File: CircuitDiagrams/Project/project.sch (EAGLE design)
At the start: 19 parts, among them IC1 UC3C, IC2 PCA9542A, IC3 MT48LC4M16A2TSOP54, Q1 OV7670, Q2 OV7670, X1 SDBMF

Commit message: Done some more to the PCB. Worked out how to use the cam2print script
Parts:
- added C1, C2: 22pF, passives:C-EUC1206
- added C3, C4: 10uF, passives:CPOL-EUSMCE
- added IC4, IC5: TB6593FNGSSOP20, ICs:TB6593FNGSSOP20
- added J2, J3: 1BY2THROUGHHOLE, Headers:1BY2THROUGHHOLE
- added Q3: VREGSOT-223, Semiconductors:VREGSOT-223
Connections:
- removed net VBUS: IC1.VBUS, U$1.VBUS
- new net +5V: C4.+, IC1.VBUS, Q3.VIN, U$1.VBUS
- new net N$1: IC5.O1, IC5.O11, J3.1
- new net N$2: IC5.O2, IC5.O22, J3.2
- new net N$3: IC4.O2, IC4.O22, J2.2
- new net N$4: IC4.O1, IC4.O11, J2.1
- net +3V3: now also C3.+, IC4.VCC, IC4.VM1, IC4.VM2, IC4.VM3, IC4.VM4, IC5.VCC, IC5.VM1, IC5.VM2, IC5.VM3, IC5.VM4, Q3.VOUT
- net GND: now also C3.-, C4.-, IC4.GND, IC4.PGND1, IC4.PGND2, IC4.PGND3, IC4.PGND4, IC4.PGND5, IC4.PGND6, IC5.GND, IC5.PGND1, IC5.PGND2, IC5.PGND3, IC5.PGND4, IC5.PGND5, IC5.PGND6, Q3.GND
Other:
- note added: "Motor Drivers"
- note added: "SDRAM"
- note added: "Voltage Regulator"

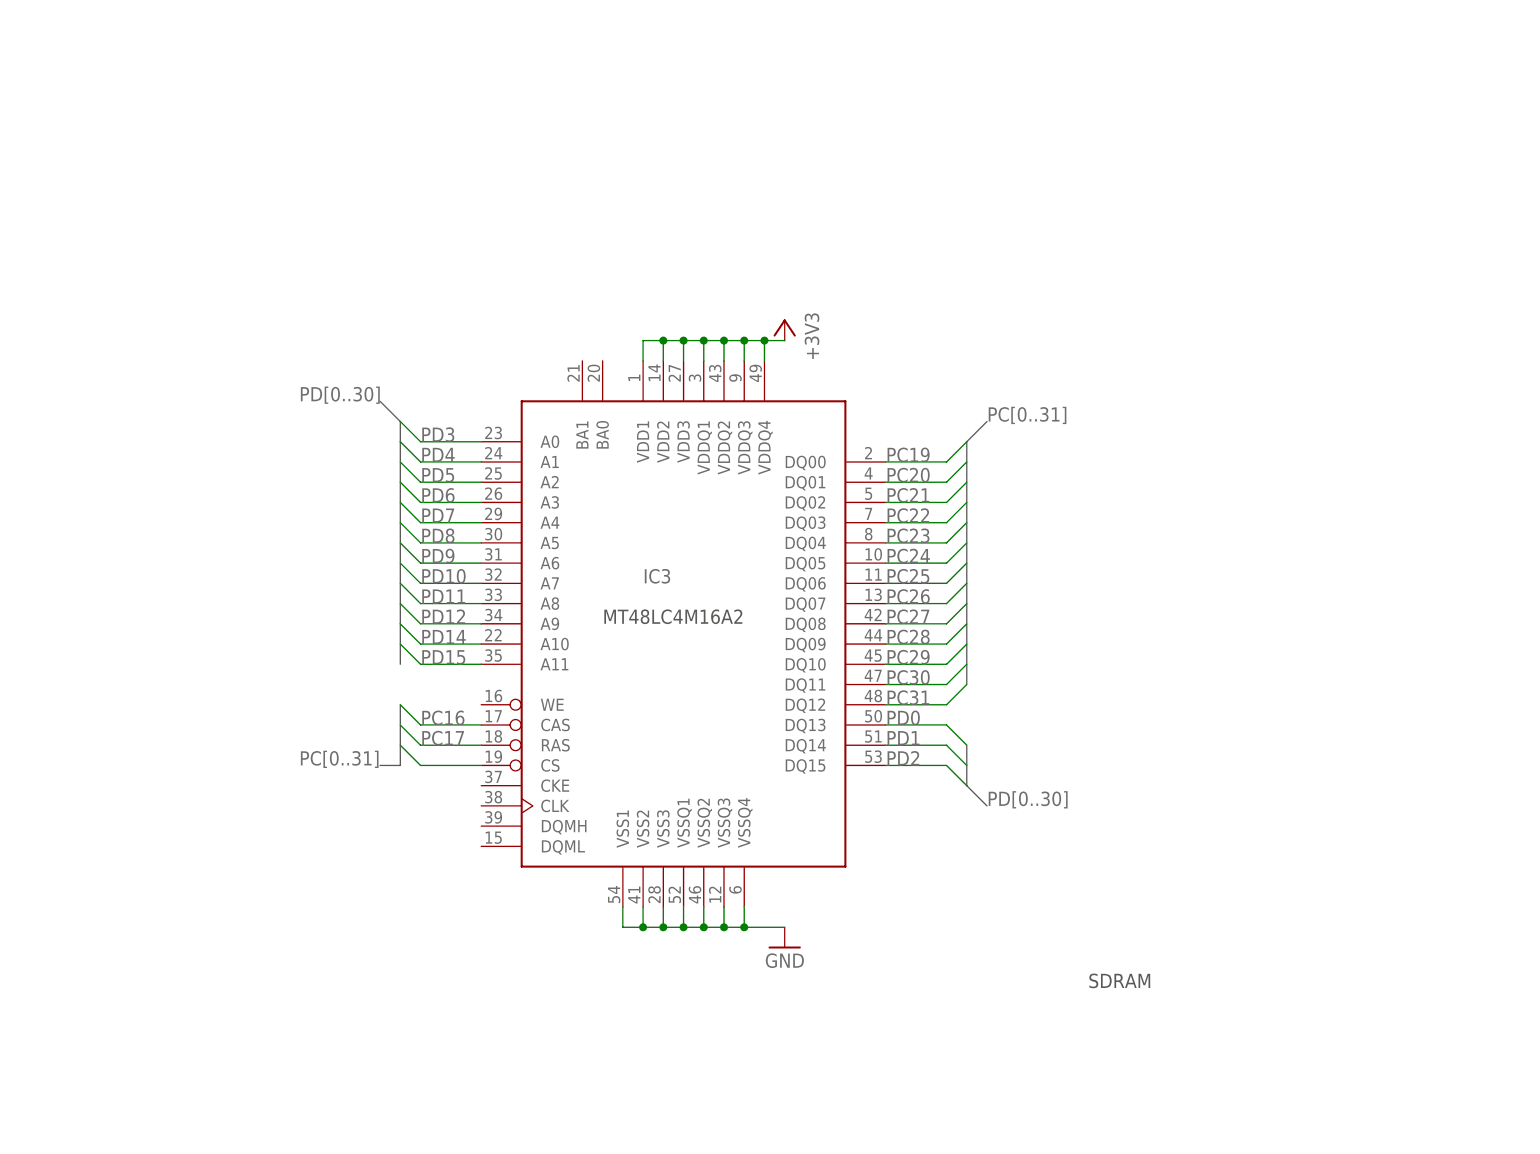
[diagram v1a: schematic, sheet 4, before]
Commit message: Added more to the ciruit diagram and PCB. Checked that made components are correct
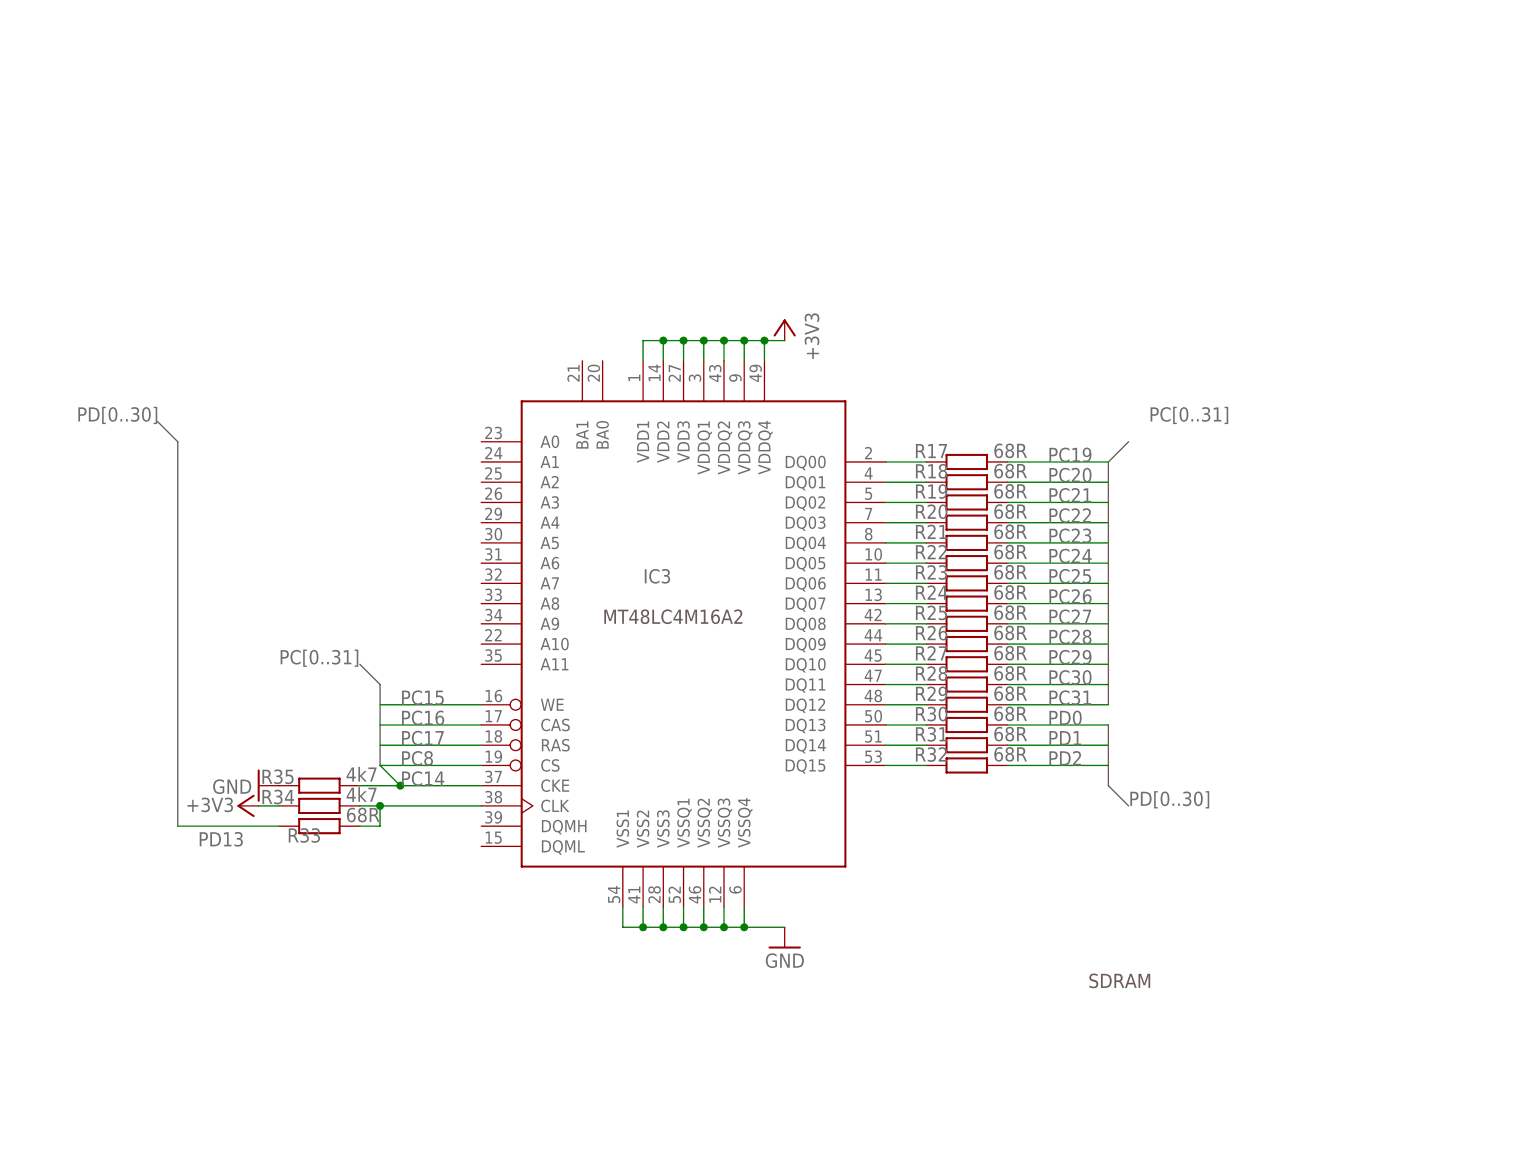
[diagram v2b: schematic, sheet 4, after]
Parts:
- removed X1: SDBMF, Misc:SDBMF
- added Q4, Q5: TCRT1010TH, Sensors:TCRT1010TH
- added R11, R13: 150, passives:R0603
- added R12, R14: 10k, passives:R0603
- added R15, R16: (no value), SparkFun:POTTRIM
- added R17, R18, R19, R20, R21, R22, R23, R24, R25, R26, R27, R28, R29, R30, R31, R32, R33: 68R, passives:R0603
- added R34, R35: 4k7, passives:R0603
- added X2: MICROSDSMD, Misc:MICROSDSMD
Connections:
- new net MOTOR_REF_1: R15.S
- new net MOTOR_REF_2: R16.S
- new net MOTOR_SENSE_1: Q4.COLLECTOR, R12.1
- new net MOTOR_SENSE_2: Q5.COLLECTOR, R14.1
- new net N$10: IC3.DQ03, R20.1
- new net N$11: IC3.DQ04, R21.1
- new net N$12: IC3.DQ05, R22.1
- new net N$13: IC3.DQ06, R23.1
- new net N$14: IC3.DQ07, R24.1
- new net N$15: IC3.DQ08, R25.1
- new net N$16: IC3.DQ09, R26.1
- new net N$17: IC3.DQ10, R27.1
- new net N$18: IC3.DQ11, R28.1
- new net N$19: IC3.DQ12, R29.1
- new net N$20: IC3.DQ13, R30.1
- new net N$21: IC3.DQ14, R31.1
- new net N$22: IC3.DQ15, R32.1
- new net N$24: IC3.CLK, R33.2, R34.2
- new net N$5: Q4.ANODE, R11.1
- new net N$6: Q5.ANODE, R13.1
- new net N$7: IC3.DQ00, R17.1
- new net N$8: IC3.DQ01, R18.1
- new net N$9: IC3.DQ02, R19.1
- net +3V3: now also R11.2, R12.2, R13.2, R14.2, R15.E, R16.E, R34.1, X2.VDD; no longer X1.VDD
- net GND: now also Q4.CATHODE, Q4.EMMITTER, Q5.CATHODE, Q5.EMMITTER, R15.A, R16.A, R35.1, X2.VSS; no longer X1.VSS, X1.VSS2
- net PB10: now also X2.DI; no longer X1.DI
- net PB11: now also X2.DO; no longer X1.DO
- net PB12: now also X2.CLK; no longer X1.CLK
- net PB13: now also X2.NCS; no longer X1.NCS
- net PC14: now also IC3.CKE, R35.2
- net PC15: now also IC3.WE
- net PC19: now also R17.2; no longer IC3.DQ00
- net PC20: now also R18.2; no longer IC3.DQ01
- net PC21: now also R19.2; no longer IC3.DQ02
- net PC22: now also R20.2; no longer IC3.DQ03
- net PC23: now also R21.2; no longer IC3.DQ04
- net PC24: now also R22.2; no longer IC3.DQ05
- net PC25: now also R23.2; no longer IC3.DQ06
- net PC26: now also R24.2; no longer IC3.DQ07
- net PC27: now also R25.2; no longer IC3.DQ08
- net PC28: now also R26.2; no longer IC3.DQ09
- net PC29: now also R27.2; no longer IC3.DQ10
- net PC30: now also R28.2; no longer IC3.DQ11
- net PC31: now also R29.2; no longer IC3.DQ12
- net PD0: now also R30.2; no longer IC3.DQ13
- net PD1: now also R31.2; no longer IC3.DQ14
- net PD10: no longer IC3.A7
- net PD11: no longer IC3.A8
- net PD12: no longer IC3.A9
- net PD13: now also R33.1
- net PD14: no longer IC3.A10
- net PD15: no longer IC3.A11
- net PD2: now also R32.2; no longer IC3.DQ15
- net PD3: no longer IC3.A0
- net PD4: no longer IC3.A1
- net PD5: no longer IC3.A2
- net PD6: no longer IC3.A3
- net PD7: no longer IC3.A4
- net PD8: no longer IC3.A5
- net PD9: no longer IC3.A6
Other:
- note added: "Motor Sensors"

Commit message: Done some more on PCB, mainly adding decoupling capacitors (lots of)
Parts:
- added C10, C8: 4.7u, passives:C-EUC1206
- added C11, C13, C15, C17, C20: 33n, passives:C-EUC1206
- added C12, C14, C16, C19, C21, C7: 100n, passives:C-EUC1206
- added C18, C24, C27, C29, C32, C33, C42: 100n, passives:C-EUC0603
- added C22, C25, C28, C30, C43, C9: 33n, passives:C-EUC0603
- added C23, C26: 4.7u, passives:C-EUC0603
- added C34, C36, C38, C39: 0.1u, passives:C-EUC0603
- added C35, C37, C40, C41: 10u, passives:CPOL-EUSMCZ
- added C5: 2.2u, passives:C-EUC1206
- added C6: 1n, passives:C-EUC1206
- added Q6: CSM-7X-DU, crystal:CSM-7X-DU
- added R36: 1k5, passives:R0603
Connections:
- new net ADCREFN: C21.2, C22.2, IC1.ADCREFN
- new net ADCREFP: C21.1, C22.1, IC1.ADCREFP
- new net N$32: R36.1, X2.CD
- new net VDDCORE: IC1.VDDCORE
- net +3V3: now also C10.1, C11.1, C12.1, C13.1, C14.1, C15.1, C16.1, C17.1, C18.1, C19.1, C20.1, C23.1, C24.1, C25.1, C26.1, C27.1, C28.1, C29.1, C30.1, C32.1, C33.1, C34.1, C35.+, C36.1, C37.+, C38.1, C39.1, C40.+, C41.+, C42.1, C43.1, C5.1, C6.1, C7.1, C8.1, C9.1
- net GND: now also C1.2, C10.2, C11.2, C12.2, C13.2, C14.2, C15.2, C16.2, C17.2, C18.2, C19.2, C2.2, C20.2, C23.2, C24.2, C25.2, C26.2, C27.2, C28.2, C29.2, C30.2, C32.2, C33.2, C34.2, C35.-, C36.2, C37.-, C38.2, C39.2, C40.-, C41.-, C42.2, C43.2, C5.2, C6.2, C7.2, C8.2, C9.2, X2.SW
- net PB0: now also C2.1, Q6.1
- net PB1: now also C1.1, Q6.2
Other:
- note added: "Close to ADCREFP / ADCREFN"
- note added: "Close to VDD/GND CORE"
- note added: "Close to VDDANA/GNDANA"
- note added: "Close to VDDIN/GNDCORE pairs"
- note added: "Close to VDDIO/GND Pairs"
- note added: "Crystal"
- note added: "Decoupling Capacitors"
- note added: "Decoupling Capacitors - Place near VDD/VSS Pairs"
- note added: "Decoupling Capcitors"
- note added: "Near VCC"
- note added: "Near VM"
- moved on the sheet: C2, IC4, IC5, J2, J3, Q4, Q5, R11, R12, R13, R14, R15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

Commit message: Placed all components. Need to confirm the circuit diagram and complete that before routing
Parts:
- C1, C10, C11, C12, C13, C14, C15, C16, C17, C19, C2, C20, C21, C5, C6, C7, C8: device passives:C-EUC1206 -> passives:C-EUC0603
- C3, C4: device passives:CPOL-EUSMCE -> passives:CPOL-EUSMCP
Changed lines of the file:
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@@
 <part name="Q3" library="Semiconductors" deviceset="VREG" device="SOT-223"/>
 <part name="GND13" library="supply1" deviceset="GND" device=""/>
-<part name="C1" library="passives" deviceset="C-EU" device="C1206" value="22pF"/>
-<part name="C2" library="passives" deviceset="C-EU" device="C1206" value="22pF"/>
-<part name="C3" library="passives" deviceset="CPOL-EU" device="SMCE" value="10uF"/>
-<part name="C4" library="passives" deviceset="CPOL-EU" device="SMCE" value="10uF"/>
+<part name="C1" library="passives" deviceset="C-EU" device="C0603" value="22pF"/>
+<part name="C2" library="passives" deviceset="C-EU" device="C0603" value="22pF"/>
+<part name="C3" library="passives" deviceset="CPOL-EU" device="SMCP" value="10uF"/>
+<part name="C4" library="passives" deviceset="CPOL-EU" device="SMCP" value="10uF"/>
 <part name="+3V15" library="supply1" deviceset="+3V3" device=""/>
 <part name="P+1" library="supply1" deviceset="+5V" device=""/>
@@
 <part name="Q6" library="crystal" deviceset="CSM-7X-DU" device=""/>
 <part name="GND19" library="supply1" deviceset="GND" device=""/>
-<part name="C5" library="passives" deviceset="C-EU" device="C1206" value="2.2u"/>
-<part name="C6" library="passives" deviceset="C-EU" device="C1206" value="1n"/>
-<part name="C7" library="passives" deviceset="C-EU" device="C1206" value="100n"/>
-<part name="C8" library="passives" deviceset="C-EU" device="C1206" value="4.7u"/>
+<part name="C5" library="passives" deviceset="C-EU" device="C0603" value="2.2u"/>
+<part name="C6" library="passives" deviceset="C-EU" device="C0603" value="1n"/>
+<part name="C7" library="passives" deviceset="C-EU" device="C0603" value="100n"/>
+<part name="C8" library="passives" deviceset="C-EU" device="C0603" value="4.7u"/>
 <part name="C9" library="passives" deviceset="C-EU" device="C0603" value="33n"/>
-<part name="C10" library="passives" deviceset="C-EU" device="C1206" value="4.7u"/>
-<part name="C11" library="passives" deviceset="C-EU" device="C1206" value="33n"/>
-<part name="C12" library="passives" deviceset="C-EU" device="C1206" value="100n"/>
-<part name="C13" library="passives" deviceset="C-EU" device="C1206" value="33n"/>
-<part name="C14" library="passives" deviceset="C-EU" device="C1206" value="100n"/>
-<part name="C15" library="passives" deviceset="C-EU" device="C1206" value="33n"/>
-<part name="C16" library="passives" deviceset="C-EU" device="C1206" value="100n"/>
-<part name="C17" library="passives" deviceset="C-EU" device="C1206" value="33n"/>
+<part name="C10" library="passives" deviceset="C-EU" device="C0603" value="4.7u"/>
+<part name="C11" library="passives" deviceset="C-EU" device="C0603" value="33n"/>
+<part name="C12" library="passives" deviceset="C-EU" device="C0603" value="100n"/>
+<part name="C13" library="passives" deviceset="C-EU" device="C0603" value="33n"/>
+<part name="C14" library="passives" deviceset="C-EU" device="C0603" value="100n"/>
+<part name="C15" library="passives" deviceset="C-EU" device="C0603" value="33n"/>
+<part name="C16" library="passives" deviceset="C-EU" device="C0603" value="100n"/>
+<part name="C17" library="passives" deviceset="C-EU" device="C0603" value="33n"/>
 <part name="C18" library="passives" deviceset="C-EU" device="C0603" value="100n"/>
-<part name="C19" library="passives" deviceset="C-EU" device="C1206" value="100n"/>
-<part name="C20" library="passives" deviceset="C-EU" device="C1206" value="33n"/>
-<part name="C21" library="passives" deviceset="C-EU" device="C1206" value="100n"/>
+<part name="C19" library="passives" deviceset="C-EU" device="C0603" value="100n"/>
+<part name="C20" library="passives" deviceset="C-EU" device="C0603" value="33n"/>
+<part name="C21" library="passives" deviceset="C-EU" device="C0603" value="100n"/>
 <part name="C22" library="passives" deviceset="C-EU" device="C0603" value="33n"/>
 <part name="GND20" library="supply1" deviceset="GND" device=""/>

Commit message: Wired up GPIOs to Devices. Need to add a UI.
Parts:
- added C31: 100n, passives:C-EUC0603
- added D1: DIODESMD, Semiconductors:DIODESMD
- added J4: 1BY2THROUGHHOLE, Headers:1BY2THROUGHHOLE
- added R37, R38, R39, R40: 68R, passives:R0603
- added R41: 100k, passives:R0603
- added R42, R43: 39R, passives:R0603
- R36: value 1k5 -> 100k
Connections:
- removed net MOTOR_REF_1: R15.S
- removed net MOTOR_REF_2: R16.S
- removed net MOTOR_SENSE_1: Q4.COLLECTOR, R12.1
- removed net MOTOR_SENSE_2: Q5.COLLECTOR, R14.1
- removed net N$32: R36.1, X2.CD
- removed net OV_NOE0: Q1.NOE
- removed net OV_NOE1: Q2.NOE
- removed net OV_RCLK0: Q1.RCLK
- removed net OV_RCLK1: Q2.RCLK
- removed net OV_RRST0: Q1.RRST
- removed net OV_RRST1: Q2.RRST
- removed net OV_VSYNC0: Q1.VSYNC
- removed net OV_VSYNC1: Q2.VSYNC
- removed net OV_WEN0: Q1.WEN
- removed net OV_WEN1: Q2.WEN
- removed net OV_WRST0: Q1.WRST
- removed net OV_WRST1: Q2.WRST
- new net N$23: R37.2, R41.2, X2.NCS
- new net N$25: R38.2, X2.DI
- new net N$26: R39.2, X2.CLK
- new net N$27: R40.2, X2.DO
- new net N$28: IC1.DM, R42.2
- new net N$29: IC1.DP, R43.2
- net +3V3: now also D1.ANODE, R41.1, X2.SW
- net DM: now also R42.1; no longer IC1.DM
- net DP: now also R43.1; no longer IC1.DP
- net GND: now also C31.2, R36.2; no longer X2.SW
- net PA15: now also Q1.RRST
- net PA16: now also C31.1, D1.CATHODE
- net PA19: now also Q1.RCLK
- net PA20: now also Q1.WEN
- net PA21: now also Q1.WRST
- net PA22: now also Q2.RRST
- net PA23: now also Q2.RCLK
- net PA24: now also Q2.WEN
- net PA25: now also Q2.WRST
- net PA26: now also Q2.VSYNC
- net PA27: now also Q2.NOE
- net PA28: now also Q1.NOE
- net PA29: now also Q1.VSYNC
- net PA4: now also U$1.ID
- net PA6: now also Q4.COLLECTOR, R12.1
- net PA7: now also R15.S
- net PA8: now also Q5.COLLECTOR, R14.1
- net PA9: now also R16.S
- net PB10: now also IC4.IN2; no longer X2.DI
- net PB11: now also IC4.PWM; no longer X2.DO
- net PB12: no longer X2.CLK
- net PB13: now also IC5.PWM; no longer X2.NCS
- net PB14: now also IC5.IN2
- net PB15: now also IC5.IN1
- net PB16: now also IC5.STBY
- net PB19: now also R38.1
- net PB20: now also R40.1
- net PB21: now also R39.1
- net PB25: now also R37.1
- net PB26: now also R36.1, X2.CD
- net PB8: now also IC4.STBY
- net PB9: now also IC4.IN1
- net PC2: now also J4.1
- net PC3: now also J4.2
- net PD10: now also IC3.A7
- net PD11: now also IC3.A8
- net PD12: now also IC3.A9
- net PD14: now also IC3.A10
- net PD15: now also IC3.A11
- net PD16: now also IC3.BA1
- net PD17: now also IC3.BA0
- net PD3: now also IC3.A0
- net PD4: now also IC3.A1
- net PD5: now also IC3.A2
- net PD6: now also IC3.A3
- net PD7: now also IC3.A4
- net PD8: now also IC3.A5
- net PD9: now also IC3.A6
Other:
- note added: "I2C Test Point"
